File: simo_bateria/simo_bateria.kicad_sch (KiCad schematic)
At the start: 3 parts, among them U1 simo_bateria, U2 cargador_bateria

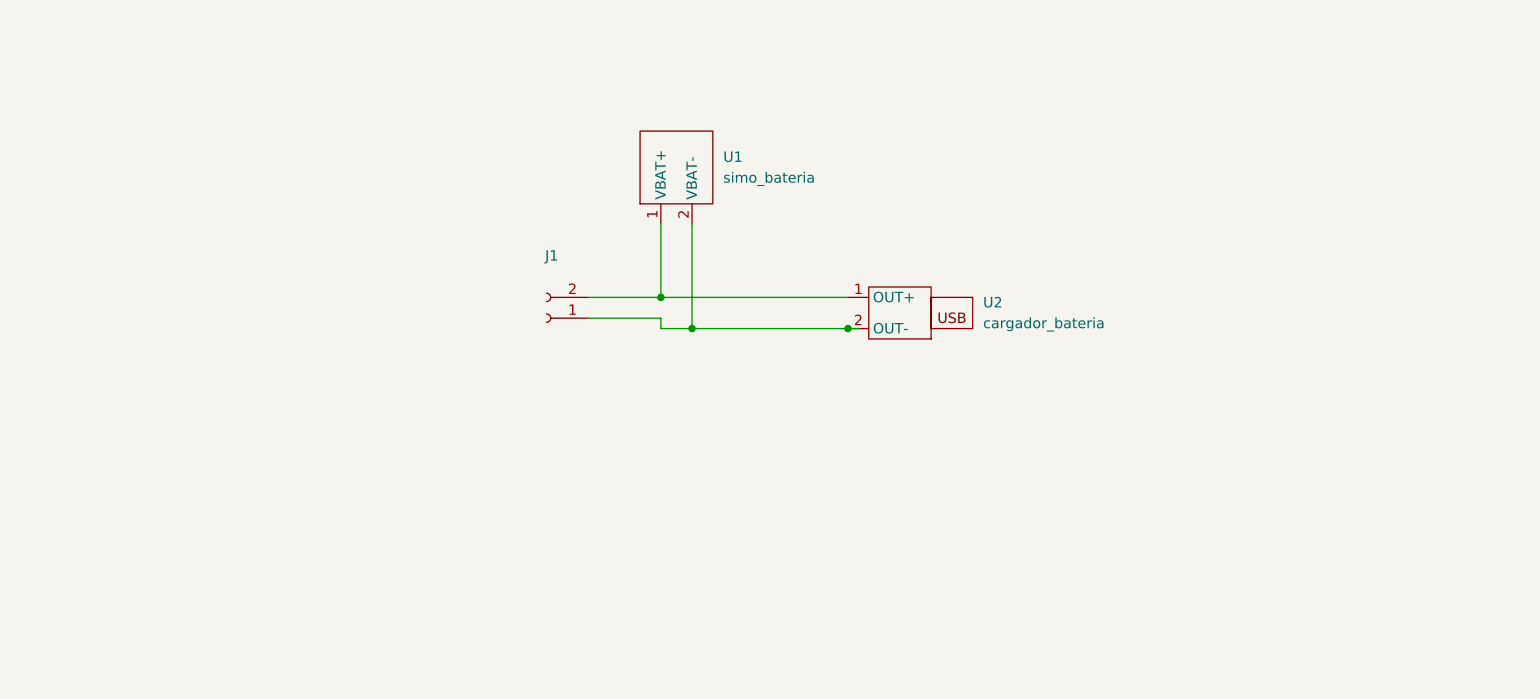
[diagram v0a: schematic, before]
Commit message: se completaron todos los modelos 3d y se verifico las footprint
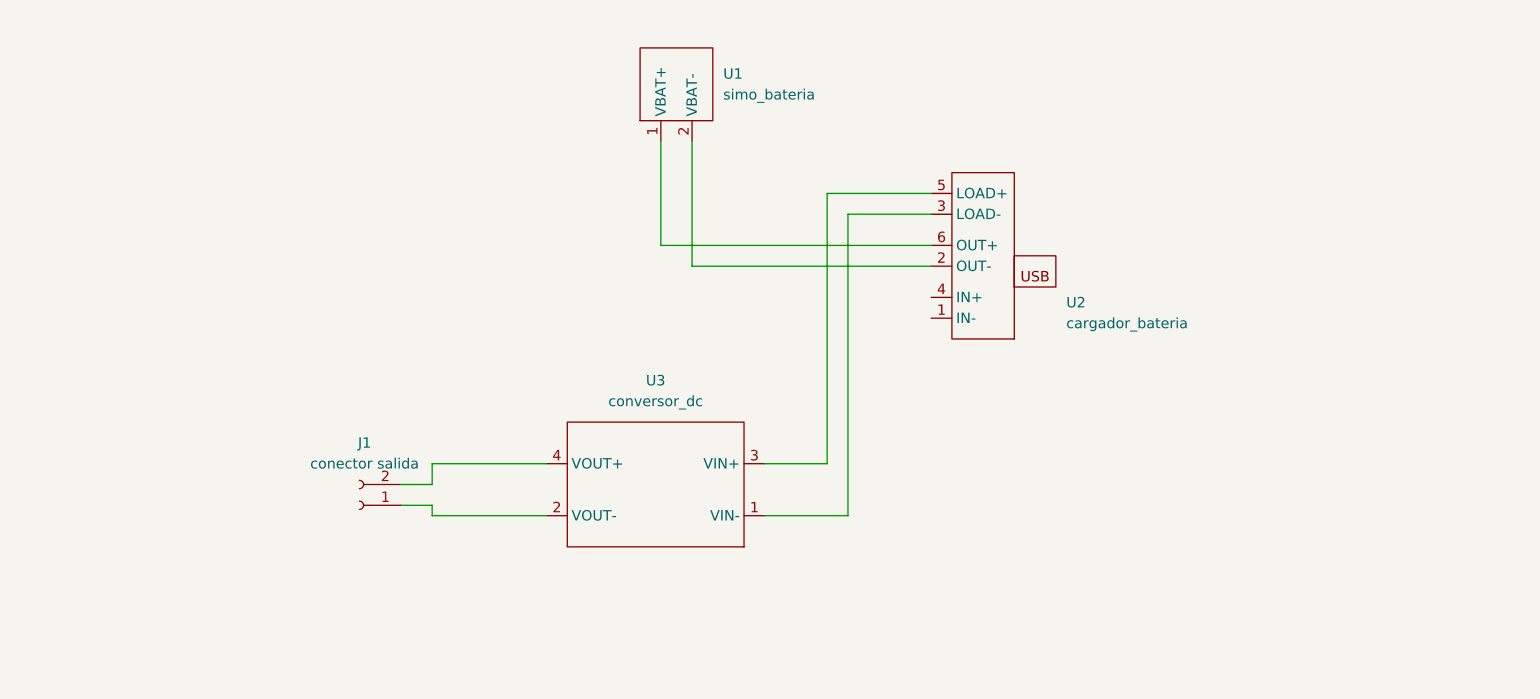
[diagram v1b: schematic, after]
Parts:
- added U3: conversor_dc, simo_bateria:conversor_dc_dc, symbol simo_shield:conversor_dc
- J1: value (none) -> conector salida; footprint (none) -> Connector_PinSocket_2.54mm:PinSocket_1x02_P2.54mm_Vertical
- U1: footprint (none) -> simo_bateria:bateria
- U2: footprint (none) -> simo_bateria:cargador_bat
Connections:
- net at U1.2 (VBAT-), U2.2 (OUT-): no longer J1.1 (Pin_1)
- new net: U1.1 (VBAT+), U2.6 (OUT+)
- new net: J1.1 (Pin_1), U3.2 (VOUT-)
- new net: J1.2 (Pin_2), U3.4 (VOUT+)
- new net: U2.3 (LOAD-), U3.1 (VIN-)
- new net: U2.5 (LOAD+), U3.3 (VIN+)
- now unconnected: U2.1 (OUT+)
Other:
- moved on the sheet: J1, U1
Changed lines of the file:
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@@
 (kicad_sch (version 20211123) (generator eeschema)
   (paper "A4")
-  (junction (at 114.3 48.26) (diameter 0) (color 0 0 0 0)
-  )
-  (junction (at 133.35 48.26) (diameter 0) (color 0 0 0 0)
-  )
-  (junction (at 110.49 44.45) (diameter 0) (color 0 0 0 0)
-  )
-  (wire (pts (xy 110.49 35.56) (xy 110.49 44.45))
+  (wire (pts (xy 114.3 25.4) (xy 114.3 40.64))
     (stroke (width 0) (type default) (color 0 0 0 0))
   )
-  (wire (pts (xy 114.3 48.26) (xy 133.35 48.26))
+  (wire (pts (xy 78.74 69.85) (xy 82.55 69.85))
     (stroke (width 0) (type default) (color 0 0 0 0))
   )
-  (wire (pts (xy 101.6 46.99) (xy 110.49 46.99))
+  (wire (pts (xy 133.35 34.29) (xy 133.35 71.12))
     (stroke (width 0) (type default) (color 0 0 0 0))
   )
-  (wire (pts (xy 110.49 48.26) (xy 114.3 48.26))
+  (wire (pts (xy 123.19 64.77) (xy 130.81 64.77))
     (stroke (width 0) (type default) (color 0 0 0 0))
   )
-  (wire (pts (xy 133.35 48.26) (xy 134.62 48.26))
+  (wire (pts (xy 82.55 69.85) (xy 82.55 71.12))
     (stroke (width 0) (type default) (color 0 0 0 0))
   )
-  (wire (pts (xy 110.49 44.45) (xy 133.35 44.45))
+  (wire (pts (xy 143.51 34.29) (xy 133.35 34.29))
     (stroke (width 0) (type default) (color 0 0 0 0))
   )
-  (wire (pts (xy 110.49 46.99) (xy 110.49 48.26))
+  (wire (pts (xy 96.52 64.77) (xy 82.55 64.77))
     (stroke (width 0) (type default) (color 0 0 0 0))
   )
-  (wire (pts (xy 114.3 35.56) (xy 114.3 48.26))
+  (wire (pts (xy 123.19 71.12) (xy 133.35 71.12))
     (stroke (width 0) (type default) (color 0 0 0 0))
   )
-  (wire (pts (xy 101.6 44.45) (xy 110.49 44.45))
+  (wire (pts (xy 143.51 31.75) (xy 130.81 31.75))
     (stroke (width 0) (type default) (color 0 0 0 0))
   )
-  (symbol (lib_id "simo_shield:simo_bateria") (at 107.95 33.02 90) (unit 1)
+  (wire (pts (xy 82.55 71.12) (xy 96.52 71.12))
+    (stroke (width 0) (type default) (color 0 0 0 0))
+  )
+  (wire (pts (xy 78.74 67.31) (xy 82.55 67.31))
+    (stroke (width 0) (type default) (color 0 0 0 0))
+  )
+  (wire (pts (xy 114.3 40.64) (xy 143.51 40.64))
+    (stroke (width 0) (type default) (color 0 0 0 0))
+  )
+  (wire (pts (xy 110.49 38.1) (xy 110.49 25.4))
+    (stroke (width 0) (type default) (color 0 0 0 0))
+  )
+  (wire (pts (xy 82.55 64.77) (xy 82.55 67.31))
+    (stroke (width 0) (type default) (color 0 0 0 0))
+  )
+  (wire (pts (xy 143.51 38.1) (xy 110.49 38.1))
+    (stroke (width 0) (type default) (color 0 0 0 0))
+  )
+  (wire (pts (xy 130.81 31.75) (xy 130.81 64.77))
+    (stroke (width 0) (type default) (color 0 0 0 0))
+  )
+  (symbol (lib_id "simo_shield:simo_bateria") (at 107.95 22.86 90) (unit 1)
     (in_bom yes) (on_board yes) (fields_autoplaced)
-    (property "Reference" "U1" (id 0) (at 118.11 27.3049 90)
+    (property "Reference" "U1" (id 0) (at 118.11 17.1449 90)
       (effects (font (size 1.27 1.27)) (justify right))
     )
-    (property "Value" "simo_bateria" (id 1) (at 118.11 29.8449 90)
+    (property "Value" "simo_bateria" (id 1) (at 118.11 19.6849 90)
       (effects (font (size 1.27 1.27)) (justify right))
     )
-    (property "Footprint" "" (id 2) (at 107.95 33.02 0)
+    (property "Footprint" "simo_bateria:bateria" (id 2) (at 107.95 22.86 0)
       (effects (font (size 1.27 1.27)) hide)
     )
-    (property "Datasheet" "" (id 3) (at 107.95 33.02 0)
+    (property "Datasheet" "" (id 3) (at 107.95 22.86 0)
       (effects (font (size 1.27 1.27)) hide)
     )
@@
     (pin "2")
   )
-  (symbol (lib_id "Connector:Conn_01x02_Female") (at 96.52 46.99 180) (unit 1)
+  (symbol (lib_id "Connector:Conn_01x02_Female") (at 73.66 69.85 180) (unit 1)
     (in_bom yes) (on_board yes) (fields_autoplaced)
-    (property "Reference" "J1" (id 0) (at 97.155 39.37 0))
-    (property "Value" "" (id 1) (at 97.155 41.91 0))
-    (property "Footprint" "" (id 2) (at 96.52 46.99 0)
+    (property "Reference" "J1" (id 0) (at 74.295 62.23 0))
+    (property "Value" "conector salida" (id 1) (at 74.295 64.77 0))
+    (property "Footprint" "Connector_PinSocket_2.54mm:PinSocket_1x02_P2.54mm_Vertical" (id 2) (at 73.66 69.85 0)
       (effects (font (size 1.27 1.27)) hide)
     )
-    (property "Datasheet" "~" (id 3) (at 96.52 46.99 0)
+    (property "Datasheet" "~" (id 3) (at 73.66 69.85 0)
       (effects (font (size 1.27 1.27)) hide)
     )
@@
     (pin "2")
   )
-  (symbol (lib_id "simo_shield:cargador_bateria") (at 143.51 49.53 180) (unit 1)
+  (symbol (lib_id "simo_shield:conversor_dc") (at 120.65 74.93 180) (unit 1)
     (in_bom yes) (on_board yes) (fields_autoplaced)
-    (property "Reference" "U2" (id 0) (at 149.86 45.0849 0)
-      (effects (font (size 1.27 1.27)) (justify right))
-    )
-    (property "Value" "cargador_bateria" (id 1) (at 149.86 47.6249 0)
-      (effects (font (size 1.27 1.27)) (justify right))
-    )
-    (property "Footprint" "" (id 2) (at 143.51 49.53 0)
+    (property "Reference" "U3" (id 0) (at 109.855 54.61 0))
+    (property "Value" "conversor_dc" (id 1) (at 109.855 57.15 0))
+    (property "Footprint" "simo_bateria:conversor_dc_dc" (id 2) (at 120.65 74.93 0)
       (effects (font (size 1.27 1.27)) hide)
     )
-    (property "Datasheet" "" (id 3) (at 143.51 49.53 0)
+    (property "Datasheet" "" (id 3) (at 120.65 74.93 0)
       (effects (font (size 1.27 1.27)) hide)
     )
     (pin "1")
     (pin "2")
+    (pin "3")
+    (pin "4")
+  )
+  (symbol (lib_id "simo_shield:cargador_bateria") (at 153.67 49.53 180) (unit 1)
+    (in_bom yes) (on_board yes) (fields_autoplaced)
+    (property "Reference" "U2" (id 0) (at 160.02 45.0849 0)
+      (effects (font (size 1.27 1.27)) (justify right))
+    )
+    (property "Value" "cargador_bateria" (id 1) (at 160.02 47.6249 0)
+      (effects (font (size 1.27 1.27)) (justify right))
+    )
+    (property "Footprint" "simo_bateria:cargador_bat" (id 2) (at 153.67 49.53 0)
+      (effects (font (size 1.27 1.27)) hide)
+    )
+    (property "Datasheet" "" (id 3) (at 153.67 49.53 0)
+      (effects (font (size 1.27 1.27)) hide)
+    )
+    (pin "1")
+    (pin "2")
+    (pin "3")
+    (pin "4")
+    (pin "5")
+    (pin "6")
   )
   (sheet_instances
@@
   (symbol_instances
     (path "/a2640cd6-4679-46cc-8715-e2d94b0557dc"
-      (reference "J1") (unit 1) (value "conector") (footprint "Connector_PinSocket_2.54mm:PinSocket_1x02_P2.54mm_Vertical")
+      (reference "J1") (unit 1) (value "conector salida") (footprint "Connector_PinSocket_2.54mm:PinSocket_1x02_P2.54mm_Vertical")
     )
     (path "/590f98c1-ccf7-4374-aa9a-6dfca30e7789"
@@
       (reference "U2") (unit 1) (value "cargador_bateria") (footprint "simo_bateria:cargador_bat")
     )
+    (path "/a6606fe0-9f56-4500-be0d-c070c26fe4e2"
+      (reference "U3") (unit 1) (value "conversor_dc") (footprint "simo_bateria:conversor_dc_dc")
+    )
   )

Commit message: se hizo mas compacta pcb shield
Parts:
- J1: footprint Connector_PinSocket_2.54mm:PinSocket_1x02_P2.54mm_Vertical -> (none)
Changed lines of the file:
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@@
     (property "Reference" "J1" (id 0) (at 74.295 62.23 0))
     (property "Value" "conector salida" (id 1) (at 74.295 64.77 0))
-    (property "Footprint" "Connector_PinSocket_2.54mm:PinSocket_1x02_P2.54mm_Vertical" (id 2) (at 73.66 69.85 0)
+    (property "Footprint" "" (id 2) (at 73.66 69.85 0)
       (effects (font (size 1.27 1.27)) hide)
     )
@@
   (symbol_instances
     (path "/a2640cd6-4679-46cc-8715-e2d94b0557dc"
-      (reference "J1") (unit 1) (value "conector salida") (footprint "Connector_PinSocket_2.54mm:PinSocket_1x02_P2.54mm_Vertical")
+      (reference "J1") (unit 1) (value "conector salida") (footprint "Connector_JST:JST_EH_B2B-EH-A_1x02_P2.50mm_Vertical")
     )
     (path "/590f98c1-ccf7-4374-aa9a-6dfca30e7789"

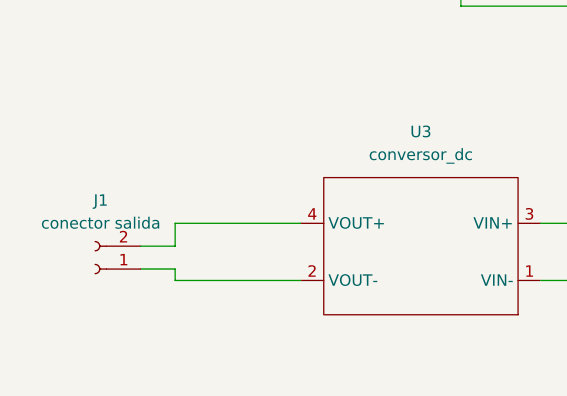
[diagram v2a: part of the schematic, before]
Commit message: se agrego conector de bateria a ambas placas
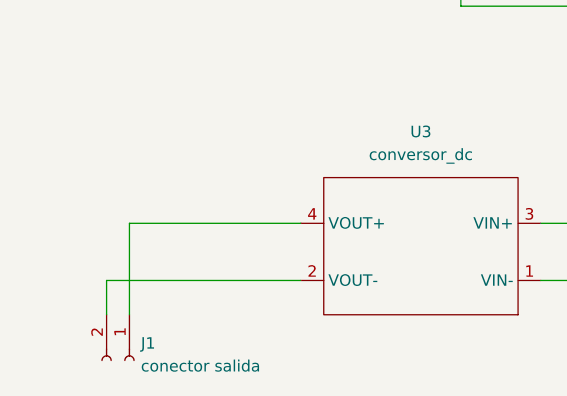
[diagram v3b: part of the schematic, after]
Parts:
- J1: footprint (none) -> Connector_JST:JST_EH_B2B-EH-A_1x02_P2.50mm_Vertical
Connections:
- net at J1.1 (Pin_1): now also U3.4 (VOUT+); no longer U3.2 (VOUT-)
- net at J1.2 (Pin_2): now also U3.2 (VOUT-); no longer U3.4 (VOUT+)
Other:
- moved on the sheet: J1
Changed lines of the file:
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@@
-    (stroke (width 0) (type default) (color 0 0 0 0))
-  )
-  (wire (pts (xy 78.74 69.85) (xy 82.55 69.85))
     (stroke (width 0) (type default) (color 0 0 0 0))
   )
@@
     (stroke (width 0) (type default) (color 0 0 0 0))
   )
-  (wire (pts (xy 82.55 69.85) (xy 82.55 71.12))
-    (stroke (width 0) (type default) (color 0 0 0 0))
-  )
   (wire (pts (xy 143.51 34.29) (xy 133.35 34.29))
     (stroke (width 0) (type default) (color 0 0 0 0))
   )
-  (wire (pts (xy 96.52 64.77) (xy 82.55 64.77))
+  (wire (pts (xy 77.47 64.77) (xy 77.47 74.93))
     (stroke (width 0) (type default) (color 0 0 0 0))
   )
@@
     (stroke (width 0) (type default) (color 0 0 0 0))
   )
-  (wire (pts (xy 82.55 71.12) (xy 96.52 71.12))
+  (wire (pts (xy 114.3 40.64) (xy 143.51 40.64))
     (stroke (width 0) (type default) (color 0 0 0 0))
   )
-  (wire (pts (xy 78.74 67.31) (xy 82.55 67.31))
+  (wire (pts (xy 96.52 64.77) (xy 77.47 64.77))
     (stroke (width 0) (type default) (color 0 0 0 0))
   )
-  (wire (pts (xy 114.3 40.64) (xy 143.51 40.64))
+  (wire (pts (xy 74.93 74.93) (xy 74.93 71.12))
     (stroke (width 0) (type default) (color 0 0 0 0))
   )
@@
     (stroke (width 0) (type default) (color 0 0 0 0))
   )
-  (wire (pts (xy 82.55 64.77) (xy 82.55 67.31))
+  (wire (pts (xy 143.51 38.1) (xy 110.49 38.1))
     (stroke (width 0) (type default) (color 0 0 0 0))
   )
-  (wire (pts (xy 143.51 38.1) (xy 110.49 38.1))
+  (wire (pts (xy 74.93 71.12) (xy 96.52 71.12))
     (stroke (width 0) (type default) (color 0 0 0 0))
   )
@@
     (pin "2")
   )
-  (symbol (lib_id "Connector:Conn_01x02_Female") (at 73.66 69.85 180) (unit 1)
+  (symbol (lib_id "Connector:Conn_01x02_Female") (at 77.47 80.01 270) (unit 1)
     (in_bom yes) (on_board yes) (fields_autoplaced)
-    (property "Reference" "J1" (id 0) (at 74.295 62.23 0))
-    (property "Value" "conector salida" (id 1) (at 74.295 64.77 0))
-    (property "Footprint" "" (id 2) (at 73.66 69.85 0)
+    (property "Reference" "J1" (id 0) (at 78.74 78.1049 90)
+      (effects (font (size 1.27 1.27)) (justify left))
+    )
+    (property "Value" "conector salida" (id 1) (at 78.74 80.6449 90)
+      (effects (font (size 1.27 1.27)) (justify left))
+    )
+    (property "Footprint" "Connector_JST:JST_EH_B2B-EH-A_1x02_P2.50mm_Vertical" (id 2) (at 77.47 80.01 0)
       (effects (font (size 1.27 1.27)) hide)
     )
-    (property "Datasheet" "~" (id 3) (at 73.66 69.85 0)
+    (property "Datasheet" "~" (id 3) (at 77.47 80.01 0)
       (effects (font (size 1.27 1.27)) hide)
     )

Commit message: simo_bateria
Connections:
- net +3V3: now reaches J1.1 (Pin_1), U3.4 (VOUT+)
- net GND: now reaches J1.2 (Pin_2), U3.2 (VOUT-)
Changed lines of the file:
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@@
 (kicad_sch (version 20211123) (generator eeschema)
   (paper "A4")
+  (junction (at 74.93 71.12) (diameter 0) (color 0 0 0 0)
+  )
+  (junction (at 77.47 64.77) (diameter 0) (color 0 0 0 0)
+  )
   (wire (pts (xy 114.3 25.4) (xy 114.3 40.64))
     (stroke (width 0) (type default) (color 0 0 0 0))
@@
     (stroke (width 0) (type default) (color 0 0 0 0))
   )
+  (wire (pts (xy 68.58 80.01) (xy 68.58 71.12))
+    (stroke (width 0) (type default) (color 0 0 0 0))
+  )
   (wire (pts (xy 114.3 40.64) (xy 143.51 40.64))
     (stroke (width 0) (type default) (color 0 0 0 0))
@@
   )
   (wire (pts (xy 110.49 38.1) (xy 110.49 25.4))
+    (stroke (width 0) (type default) (color 0 0 0 0))
+  )
+  (wire (pts (xy 68.58 64.77) (xy 77.47 64.77))
+    (stroke (width 0) (type default) (color 0 0 0 0))
+  )
+  (wire (pts (xy 68.58 71.12) (xy 74.93 71.12))
     (stroke (width 0) (type default) (color 0 0 0 0))
   )
@@
     (pin "6")
   )
+  (symbol (lib_id "power:GND") (at 68.58 80.01 0) (unit 1)
+    (in_bom yes) (on_board yes) (fields_autoplaced)
+    (property "Reference" "#PWR0101" (id 0) (at 68.58 86.36 0)
+      (effects (font (size 1.27 1.27)) hide)
+    )
+    (property "Value" "GND" (id 1) (at 68.58 85.09 0))
+    (property "Footprint" "" (id 2) (at 68.58 80.01 0)
+      (effects (font (size 1.27 1.27)) hide)
+    )
+    (property "Datasheet" "" (id 3) (at 68.58 80.01 0)
+      (effects (font (size 1.27 1.27)) hide)
+    )
+    (pin "1")
+  )
+  (symbol (lib_id "power:+3.3V") (at 68.58 64.77 0) (unit 1)
+    (in_bom yes) (on_board yes) (fields_autoplaced)
+    (property "Reference" "#PWR0102" (id 0) (at 68.58 68.58 0)
+      (effects (font (size 1.27 1.27)) hide)
+    )
+    (property "Value" "+3.3V" (id 1) (at 68.58 59.69 0))
+    (property "Footprint" "" (id 2) (at 68.58 64.77 0)
+      (effects (font (size 1.27 1.27)) hide)
+    )
+    (property "Datasheet" "" (id 3) (at 68.58 64.77 0)
+      (effects (font (size 1.27 1.27)) hide)
+    )
+    (pin "1")
+  )
   (sheet_instances
     (path "/" (page "1"))
   )
   (symbol_instances
+    (path "/fe4f4d4b-56d0-4d37-9f6d-ef338708f40e"
+      (reference "#PWR0101") (unit 1) (value "GND") (footprint "")
+    )
+    (path "/ff06b878-b39b-4a48-b025-7adaadf92467"
+      (reference "#PWR0102") (unit 1) (value "+3.3V") (footprint "")
+    )
     (path "/a2640cd6-4679-46cc-8715-e2d94b0557dc"
       (reference "J1") (unit 1) (value "conector salida") (footprint "Connector_JST:JST_EH_B2B-EH-A_1x02_P2.50mm_Vertical")

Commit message: se actualizo la placa bateria
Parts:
- removed U1: simo_bateria, simo_bateria:bateria, symbol simo_shield:simo_bateria
- removed U2: cargador_bateria, simo_bateria:cargador_bat, symbol simo_shield:cargador_bateria
- removed U3: conversor_dc, simo_bateria:conversor_dc_dc, symbol simo_shield:conversor_dc
- added BAT1: bateria, Battery:BatteryHolder_MPD_BH-18650-PC2, symbol simo_bateria:bateria
- added U2: cargador_bateria, simo_bateria:cargador_bat, symbol simo_bateria:cargador_bateria
- added U3: conversor_dc, simo_bateria:conversor_dc_dc, symbol simo_bateria:conversor_dc
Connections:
- net GND: now also U3.4 (VOUT+)
- net +3V3 renamed +BATT
- net +BATT: now also U3.2 (VOUT-)
- new net: BAT1.1 (VBAT+), U2.6 (OUT+)
- new net: BAT1.2 (VBAT-), U2.2 (OUT-)
- new net: U2.3 (LOAD-), U3.3 (VIN+)
- new net: U2.5 (LOAD+), U3.1 (VIN-)
- no-connect marks 0 -> 2
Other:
- note added: "El cargador de baterias recibe la tension del microUSB"
- moved on the sheet: J1
